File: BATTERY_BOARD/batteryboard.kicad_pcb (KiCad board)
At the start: 2 copper layers, 95.9 x 90.2 mm, 42 parts, among them J1 KEYSTONE-1042, J10 Screw_Terminal_01x02, J11 Screw_Terminal_01x02, J12 Screw_Terminal_01x01, J2 KEYSTONE-1042, J3 KEYSTONE-1042, J4 KEYSTONE-1042, J5 KEYSTONE-1042, J6 KEYSTONE-1042, J7 JST_PH_S2B-PH-SM4, J8 Screw_Terminal_01x02, J9 Screw_Terminal_01x02, Q1 IRF7458, Q2 IRF7458, U1 R5460N233AF

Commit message: Schematic Verified
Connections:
- H1 pad 1: Net-(H1-Pad1) -> unconnected-(H1-Pad1)
- H2 pad 1: Net-(H2-Pad1) -> unconnected-(H2-Pad1)
- H3 pad 1: Net-(H3-Pad1) -> unconnected-(H3-Pad1)
- H4 pad 1: Net-(H4-Pad1) -> unconnected-(H4-Pad1)
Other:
- net class Default removed

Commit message: Battery Board Final Update
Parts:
- removed J12: Screw_Terminal_01x01, Connector_PinHeader_1.00mm:PinHeader_1x01_P1.00mm_Vertical
- removed J9: Screw_Terminal_01x02, custom-footprints:SCREWTERMINAL-3.5MM-2_LOCK
- removed REF** (x6): Fiducial_0.75mm_Mask1.5mm, Fiducial:Fiducial_0.75mm_Mask1.5mm
- removed REF**: JST_PH_B2B-PH-SM4-TB_1x02-1MP_P2.00mm_Vertical, Connector_JST:JST_PH_B2B-PH-SM4-TB_1x02-1MP_P2.00mm_Vertical
- removed Ref**: Val**, custom-footprints:pycubed_logo
- removed Ref** (x2): Val**, custom-footprints:battery_version
- added D1: DFLS130L, mainboard:PWRDI-123, F.Cu at (69.8, 106.1)
- added J13: SM02B-SFHRS-TF_LF__SN_, SamacSys_Parts:SM02BSFHRSTFLFSN, F.Cu at (90.4, 58.7)
- added J14: SM02B-SFHRS-TF_LF__SN_, SamacSys_Parts:SM02BSFHRSTFLFSN, F.Cu at (81.1, 58.7)
- added J15: SM02B-SFHRS-TF_LF__SN_, SamacSys_Parts:SM02BSFHRSTFLFSN, F.Cu at (99.7, 58.7)
- added J16: SM02B-SFHRS-TF_LF__SN_, SamacSys_Parts:SM02BSFHRSTFLFSN, F.Cu at (109.1, 58.7)
- added K1: 9-1462038-9, SamacSys_Parts:914620389, F.Cu at (81.9, 109.5)
- added Q10: IRLML2803, mainboard:SOT-23, F.Cu at (85.9, 95.6)
- added Q11: IRLML2803, mainboard:SOT-23, F.Cu at (121.4, 106.5)
- added Q3: MMBT2222AT, mainboard:SOT-23, F.Cu at (73.4, 107.0)
- added Q4: IRLML2803, mainboard:SOT-23, F.Cu at (69.7, 95.6)
- added Q5: IRLML2803, mainboard:SOT-23, F.Cu at (78.0, 95.6)
- added Q6: NDS8434, mainboard:NDS8434, F.Cu at (66.6, 88.1)
- added Q7: NDS8434, mainboard:NDS8434, F.Cu at (72.9, 88.1)
- added Q8: NDS8434, mainboard:NDS8434, F.Cu at (79.1, 88.1)
- added Q9: NDS8434, mainboard:NDS8434, F.Cu at (85.4, 88.1)
- added R10: 100k, Resistor_SMD:R_0603_1608Metric, F.Cu at (66.8, 93.9)
- added R11: 100k, Resistor_SMD:R_0603_1608Metric, F.Cu at (75.1, 93.9)
- added R12: 100k, Resistor_SMD:R_0603_1608Metric, F.Cu at (83.0, 93.8)
- added R13: 100k, Resistor_SMD:R_0603_1608Metric, F.Cu at (118.5, 104.8)
- added R14: 4.7k, Resistor_SMD:R_0603_1608Metric, F.Cu at (85.0, 99.1)
- added R15: 4.7k, Resistor_SMD:R_0603_1608Metric, F.Cu at (120.4, 110.0)
- added R16: 10k, Resistor_SMD:R_0603_1608Metric, F.Cu at (86.9, 99.1)
- added R17: 10k, Resistor_SMD:R_0603_1608Metric, F.Cu at (122.3, 110.0)
- added R5: 10k, Resistor_SMD:R_0603_1608Metric, F.Cu at (73.4, 109.7)
- added R6: 10k, Resistor_SMD:R_0603_1608Metric, F.Cu at (70.6, 99.1)
- added R7: 10k, Resistor_SMD:R_0603_1608Metric, F.Cu at (79.0, 99.1)
- added R8: 4.7k, Resistor_SMD:R_0603_1608Metric, F.Cu at (68.7, 99.1)
- added R9: 4.7k, Resistor_SMD:R_0603_1608Metric, F.Cu at (77.0, 99.1)
- J10, J8: value Screw_Terminal_01x02 -> SM02B-SFHRS-TF_LF__SN_; footprint custom-footprints:SCREWTERMINAL-3.5MM-2_LOCK -> SamacSys_Parts:SM02BSFHRSTFLFSN
- J11: value Screw_Terminal_01x02 -> F3311A7H121014E200; footprint custom-footprints:SCREWTERMINAL-3.5MM-2_LOCK -> SamacSys_Parts:F3311A7H121014E200
- J7: value JST_PH_S2B-PH-SM4 -> SM02B-SFHRS-TF_LF__SN_; footprint Connector_JST:JST_PH_S2B-PH-SM4-TB_1x02-1MP_P2.00mm_Horizontal -> SamacSys_Parts:SM02BSFHRSTFLFSN
- moved J8 62.5 mm to (66.8, 111.2), turned to 0 degrees
- moved J11 57.2 mm to (65.2, 101.0), turned to -90 degrees
- moved J6 36.2 mm to (101.1, 72.9)
- moved J7 34.6 mm to (129.2, 58.9), turned to -90 degrees
- moved TP3 27.5 mm to (116.2, 66.2)
- moved TH1 19.6 mm to (103.5, 113.2)
- moved TP4 14.5 mm to (134.7, 66.7)
- moved Q2 8.14 mm to (119.6, 87.9)
- moved R1 7.48 mm to (126.3, 100.0)
- moved J10 6.98 mm to (121.9, 58.9), turned to -90 degrees
- moved Q1 6.75 mm to (127.3, 88.0)
- moved R3 6.75 mm to (134.8, 90.6)
- moved C3 6.75 mm to (134.0, 85.4)
- moved C4 5.43 mm to (120.2, 97.8)
- moved C1 5.43 mm to (125.2, 94.5)
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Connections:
- C3 pad 2: PACK- -> GND
- J10 pad 1: PACK+ -> GND
- J10 pad 2: PACK- -> PACK+
- J11 pad 1: PACK+ -> unconnected-(J11-Pad1)
- J11 pad 2: PACK- -> unconnected-(J11-Pad2)
- J7 pad 1: PACK+ -> GND
- J7 pad 2: PACK- -> PACK+
- J8 pad 1: PACK+ -> VBATT
- J8 pad 2: PACK- -> VBATT
- Q2 pad 1: PACK- -> GND
- Q2 pad 2: PACK- -> GND
- Q2 pad 3: PACK- -> GND
- R4 pad 2: PACK- -> GND
- TH1 pad 2: PACK- -> GND
- TP3 pad 1: PACK- -> GND
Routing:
- net ENAB_BURN4: track 0.00 -> 60.3 mm, vias 0 -> 2
- net /VBURN_A_IN: track 0.00 -> 41.7 mm
- net Net-(Q11-D): track 0.00 -> 40.3 mm
- net ENAB_BURN3: track 0.00 -> 24.9 mm, vias 0 -> 2
- net BAT_THERM: track 18.0 -> 41.0 mm, vias 0 -> 1
- net BURN_RELAY_A: track 0.00 -> 16.3 mm, vias 0 -> 2
- net ENAB_BURN2: track 0.00 -> 15.4 mm
- net PACK+: track 24.2 -> 37.6 mm, vias 14 -> 18
- net Net-(Q5-D): track 0.00 -> 8.28 mm
- net Net-(K1-COIL-): track 0.00 -> 8.14 mm
- net GND: track 0.00 -> 7.73 mm
- net Net-(Q10-D): track 0.00 -> 7.73 mm
- net Net-(Q4-D): track 0.00 -> 7.41 mm
- net ENAB_BURN1: track 0.00 -> 5.01 mm
- net BM: track 60.5 -> 64.6 mm
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- added copper zone on F.Cu, net /VBURN1
- added copper zone on F.Cu, net /VBURN2
- added copper zone on F.Cu, net /VBURN3
- added copper zone on F.Cu, net /VBURN4
- added copper zone on F.Cu, net /VBURN_A_IN
- added copper zone on F.Cu, net GND
- added copper zone on F.Cu, net VBATT
- removed copper zone on F.Cu, net PACK-
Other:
- outline, holes or cut-outs redrawn
- board text added: "+ -"
- board text removed: "+"
- board text removed: "-"
- board text removed: "1. CHECK CELL POLARITY BEFORE INSTALLING IN TO PACK 2. INSTALL CELLS IN NUMERICAL ORDER AS INDICATED (J1,2,3,etc...) 3. IF 0V OUTPUT, CHECK CELL BALANCE"
- board text removed: "P-"
- board text removed: "RBF PORT SIDE"

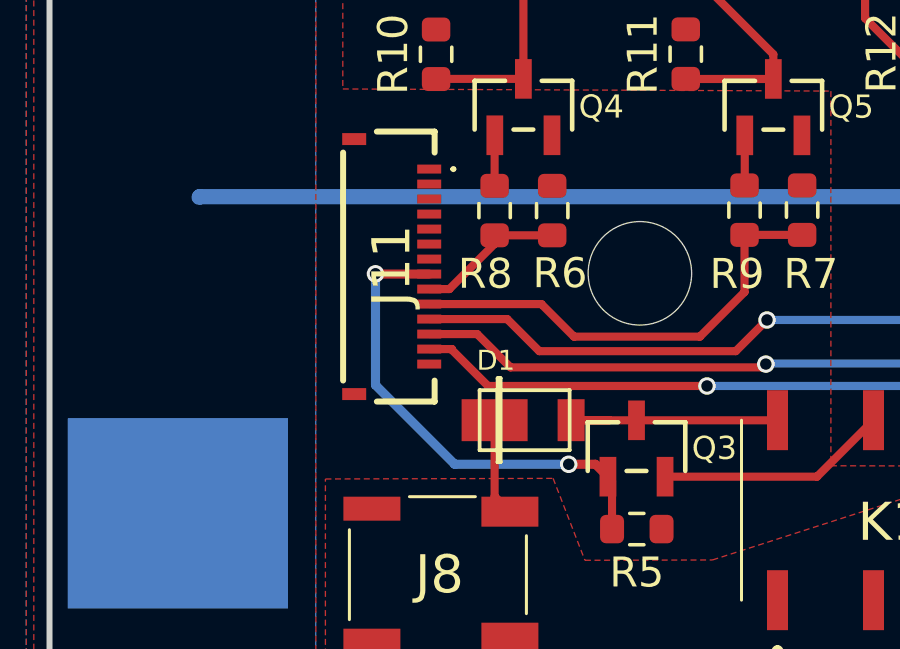
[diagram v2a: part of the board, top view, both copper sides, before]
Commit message: Updated the FPC Connections
FPC connector is reversable now
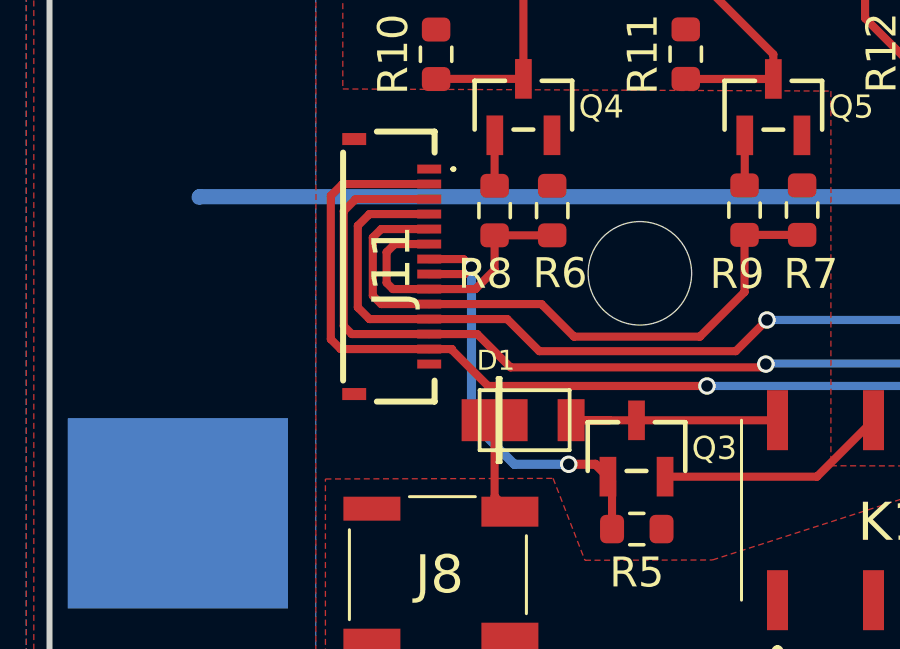
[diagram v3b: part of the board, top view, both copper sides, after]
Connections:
- J11 pad 1: unconnected-(J11-Pad1) -> GND
- J11 pad 2: unconnected-(J11-Pad2) -> BAT_THERM
- J11 pad 3: unconnected-(J11-Pad3) -> ENAB_BURN4
- J11 pad 4: unconnected-(J11-Pad4) -> ENAB_BURN3
- J11 pad 5: unconnected-(J11-Pad5) -> ENAB_BURN2
- J11 pad 6: unconnected-(J11-Pad6) -> ENAB_BURN1
- J11 pad 7: GND -> BURN_RELAY_A
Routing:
- net BAT_THERM: track 41.0 -> 52.7 mm
- net ENAB_BURN4: track 60.3 -> 70.1 mm
- net ENAB_BURN3: track 24.9 -> 32.7 mm
- net ENAB_BURN2: track 15.4 -> 21.3 mm
- net ENAB_BURN1: track 5.01 -> 9.58 mm
- net BURN_RELAY_A: track 16.3 -> 15.3 mm

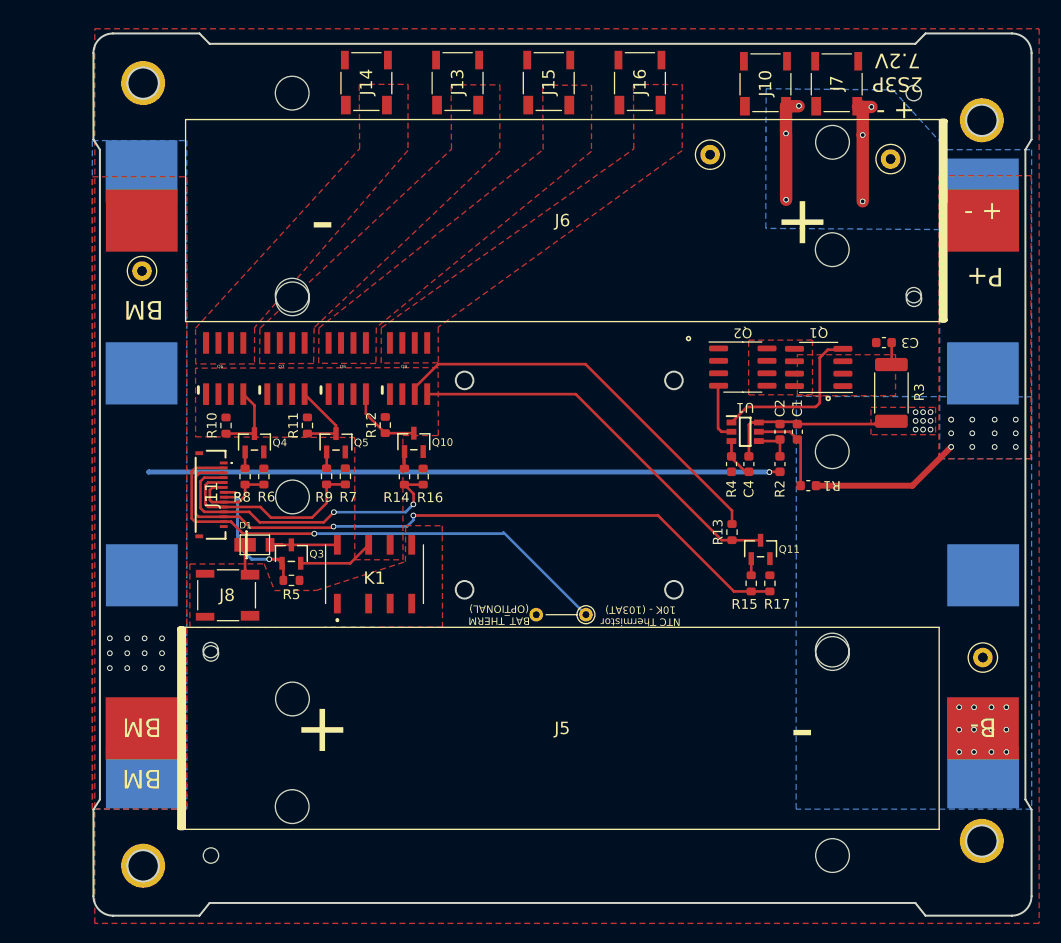
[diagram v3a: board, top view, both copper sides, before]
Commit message: Battery Board Updated based on Feedback
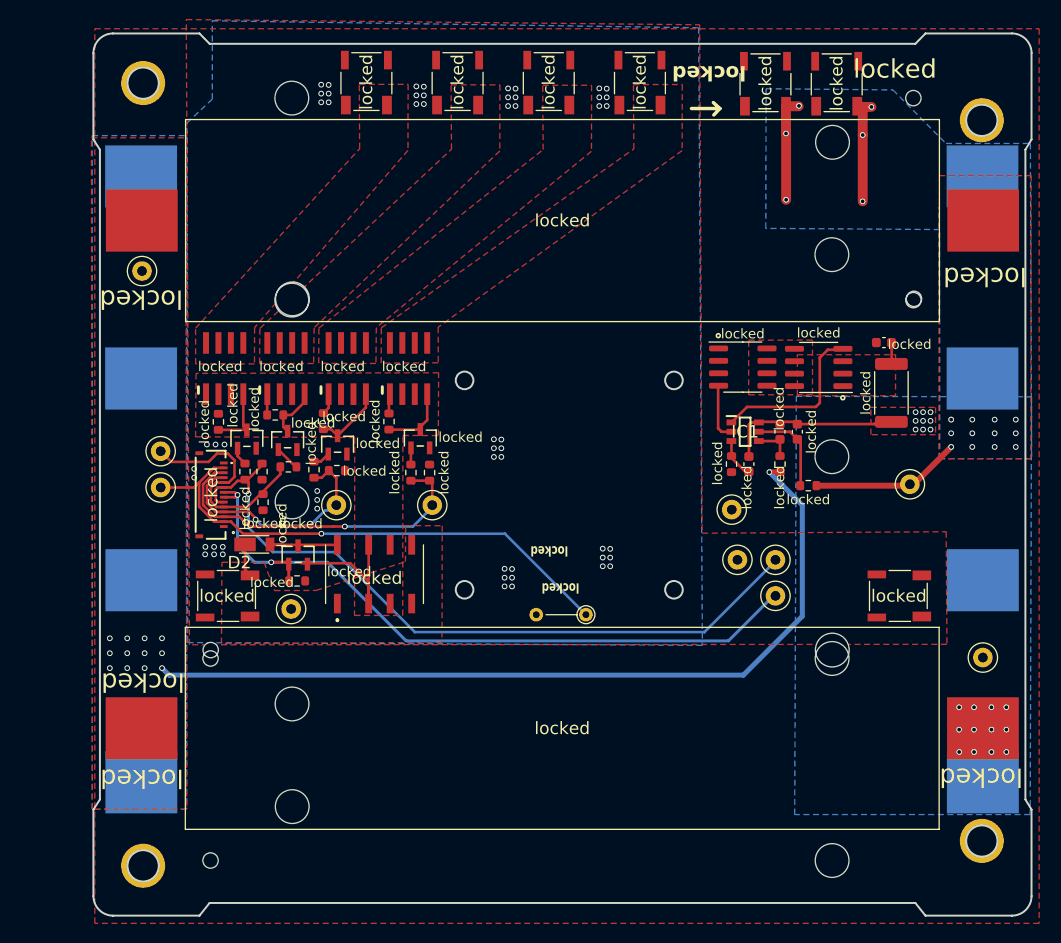
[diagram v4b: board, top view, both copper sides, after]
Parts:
- removed D1: DFLS130L, mainboard:PWRDI-123
- removed U1: R5460N233AF, custom-footprints:SOT95P280X130-6N
- added D2: DFLS130L-7, SamacSys_Parts:POWERDI_123, F.Cu at (70.3, 106.0)
- added IC1: R5460N233AF-TR-FE, SamacSys_Parts:SOT95P280X140-6N, F.Cu at (119.8, 94.5)
- added TP10: TestPoint, TestPoint:TestPoint_Loop_D1.80mm_Drill1.0mm_Beaded, F.Cu at (78.0, 102.0)
- added TP11: TestPoint, TestPoint:TestPoint_Loop_D1.80mm_Drill1.0mm_Beaded, F.Cu at (87.8, 102.0)
- added TP12: TestPoint, TestPoint:TestPoint_Loop_D1.80mm_Drill1.0mm_Beaded, F.Cu at (60.1, 100.2)
- added TP5: TestPoint, TestPoint:TestPoint_Loop_D1.80mm_Drill1.0mm_Beaded, F.Cu at (119.0, 107.6)
- added TP6: TestPoint, TestPoint:TestPoint_Loop_D1.80mm_Drill1.0mm_Beaded, F.Cu at (73.4, 112.6)
- added TP7: TestPoint, TestPoint:TestPoint_Loop_D1.80mm_Drill1.0mm_Beaded, F.Cu at (122.9, 111.3)
- added TP8: TestPoint, TestPoint:TestPoint_Loop_D1.80mm_Drill1.0mm_Beaded, F.Cu at (122.9, 107.6)
- added TP9: TestPoint, TestPoint:TestPoint_Loop_D1.80mm_Drill1.0mm_Beaded, F.Cu at (60.1, 96.5)
- added locked: SM02B-SFHRS-TF_LF__SN_, SamacSys_Parts:SM02BSFHRSTFLFSN, F.Cu at (135.5, 111.3)
- locked: renamed from J5; value KEYSTONE-1042 -> 1042; footprint custom-footprints:KEYSTONE-1042 -> SamacSys_Parts:KEYSTONE-1042
- locked: renamed from J6; value KEYSTONE-1042 -> 1042; footprint custom-footprints:KEYSTONE-1042 -> SamacSys_Parts:KEYSTONE-1042
- locked: renamed from J2; value KEYSTONE-1042 -> 1042; footprint custom-footprints:KEYSTONE-1042 -> SamacSys_Parts:KEYSTONE-1042
- locked: renamed from J1; value KEYSTONE-1042 -> 1042; footprint custom-footprints:KEYSTONE-1042 -> SamacSys_Parts:KEYSTONE-1042
- locked: renamed from J3; value KEYSTONE-1042 -> 1042; footprint custom-footprints:KEYSTONE-1042 -> SamacSys_Parts:KEYSTONE-1042
- locked: renamed from J4; value KEYSTONE-1042 -> 1042; footprint custom-footprints:KEYSTONE-1042 -> SamacSys_Parts:KEYSTONE-1042
- moved locked 36.8 mm to (83.4, 93.5)
- moved locked 36.6 mm to (85.6, 98.7)
- moved locked 36.6 mm to (87.6, 98.7)
- moved locked 36.6 mm to (86.6, 95.2)
- moved TP3 36.3 mm to (118.4, 102.5)
- moved TP4 33.3 mm to (136.7, 99.9)
- moved locked 9.27 mm to (75.7, 98.4)
- moved locked 8.84 mm to (78.1, 98.5), turned to 0 degrees
- moved locked 8.82 mm to (70.5, 101.7), turned to -90 degrees
- moved locked 7.80 mm to (78.2, 95.8)
- moved locked 6.33 mm to (76.7, 93.4)
- moved locked 4.95 mm to (73.1, 95.4)
- moved locked 4.02 mm to (73.1, 98.1), turned to 180 degrees
- moved locked 3.46 mm to (71.8, 92.8), turned to 180 degrees
- moved locked 0.86 mm to (66.0, 93.5)
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- renumbered Q1 to locked, R4 to locked, R3 to locked, J7 to locked, K1 to locked, Q6 to locked, R6 to locked, J13 to locked, R7 to locked, R16 to locked, R12 to locked, Q7 to locked, R11 to locked, J16 to locked, R13 to locked, R14 to locked, J8 to locked, Q3 to locked, R17 to locked, R15 to locked, C1 to locked, Q10 to locked, J14 to locked, J11 to locked, Q5 to locked, Q9 to locked, R10 to locked, J15 to locked, R9 to locked, Q8 to locked, C2 to locked, R5 to locked, R8 to locked, Q4 to locked, Q11 to locked, J10 to locked, C4 to locked, C3 to locked, R1 to locked, R2 to locked, Q2 to locked
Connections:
- TP3 pad 1: GND -> PACK-
- locked pad 2: GND -> PACK- (x3)
- locked pad 1: GND -> PACK- (x3)
- locked pad 3: unconnected-(J7-Pad3) -> PACK-
- locked pad 4: unconnected-(J7-Pad4) -> PACK-
- locked pad 2: unconnected-(K1-NC_1-Pad2) -> GND
- locked pad 3: unconnected-(K1-COM_1-Pad3) -> /VBURN_A_IN
- locked pad 4: unconnected-(K1-NO_1-Pad4) -> VBATT
- locked pad 3: unconnected-(J8-Pad3) -> GND
- locked pad 4: unconnected-(J8-Pad4) -> GND
- locked pad MP1: unconnected-(J11-PadMP1) -> GND
- locked pad MP2: unconnected-(J11-PadMP2) -> GND
- locked pad 3: unconnected-(J10-Pad3) -> PACK-
- locked pad 4: unconnected-(J10-Pad4) -> PACK-
- locked pad 3: GND -> PACK-
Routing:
- net ENAB_BURN1: track 9.58 -> 74.7 mm, vias 0 -> 1
- net BURN_RELAY_A: track 15.3 -> 72.8 mm
- net /VBURN_A_IN: track 41.7 -> 6.30 mm
- net ENAB_BURN4: track 70.1 -> 35.0 mm, vias 2 -> 1
- net Net-(Q11-D): track 40.3 -> 6.96 mm
- net BM: track 64.6 -> 85.5 mm
- net GND: track 7.73 -> 16.0 mm, vias 0 -> 56
- net ENAB_BURN3: track 32.7 -> 24.7 mm, vias 2 -> 1
- net ENAB_BURN2: track 21.3 -> 24.2 mm
- net Net-(Q5-D): track 8.28 -> 5.45 mm
- net BAT_THERM: track 52.7 -> 53.9 mm
- net Net-(Q5-G): track 1.67 -> 2.58 mm
- net Net-(Q4-D): track 7.41 -> 6.71 mm
- net Net-(Q10-D): track 7.73 -> 7.17 mm
- added copper zone on B.Cu, net GND
- added copper zone on F.Cu, net PACK-
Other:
- board text added: "locked"
- board text removed: "+ -"
- board text removed: "- +"
- board text removed: "2S3P 7.2V"
- board text removed: "B-"
- board text removed: "BAT_THERM (OPTIONAL)"
- board text removed: "BM"
- board text removed: "HOLLIDAY"
- board text removed: "NTC Thermistor 10K - (103AT)"
- board text removed: "P+"

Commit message: Battery Board all changes done
Based on feedback by Neil
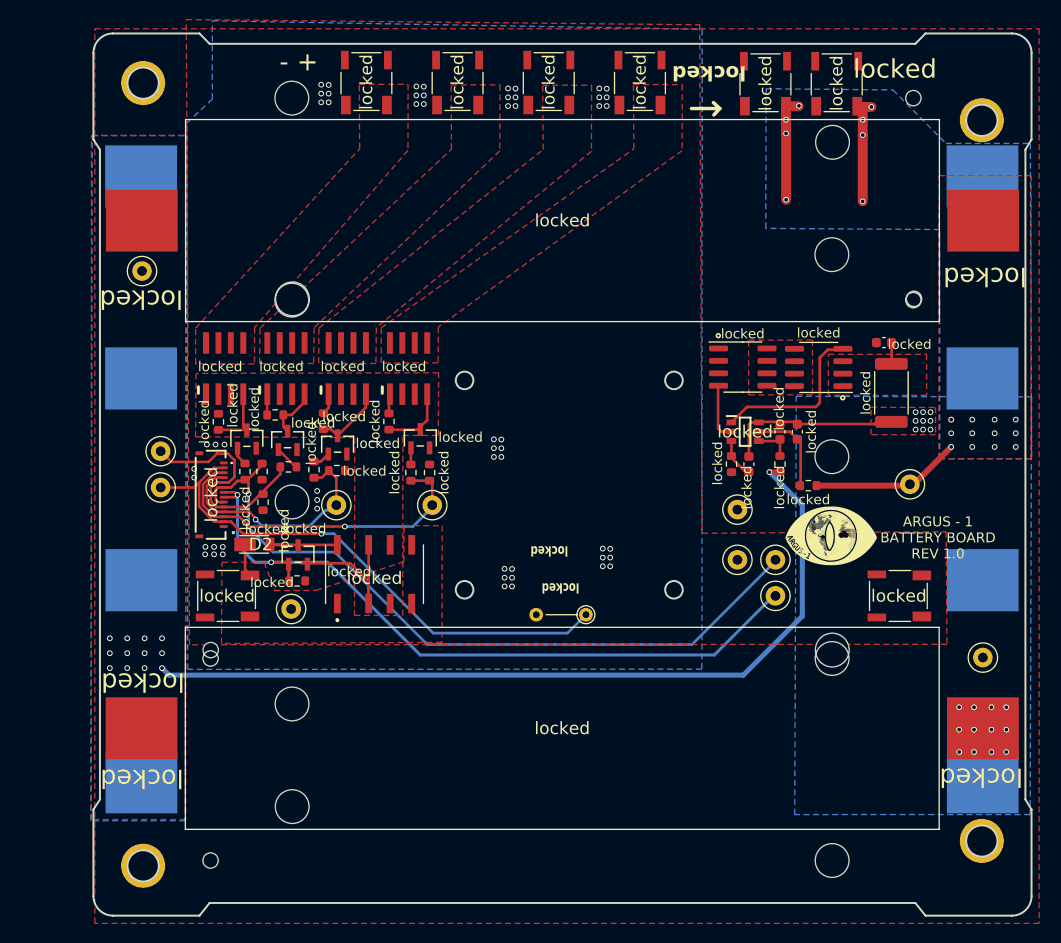
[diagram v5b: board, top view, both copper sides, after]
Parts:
- added G***: LOGO, Symbol:Argus LOGO 10x6.4, F.Cu at (128.5, 105.1)
- added G***: LOGO, Symbol:Argus LOGO 10x6.4, B.Cu at (76.4, 68.1)
- H3: moved to B.Cu
- moved TP3 0.58 mm to (119.0, 102.5)
- turned H3 to 180 degrees
- renumbered IC1 to locked
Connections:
- locked pad 3: unconnected-(J13-Pad3) -> GND
- locked pad 4: unconnected-(J13-Pad4) -> GND
- locked pad 3: unconnected-(J16-Pad3) -> GND
- locked pad 4: unconnected-(J16-Pad4) -> GND
- locked pad 3: unconnected-(J14-Pad3) -> GND
- locked pad 4: unconnected-(J14-Pad4) -> GND
- locked pad 3: unconnected-(J15-Pad3) -> GND
- locked pad 4: unconnected-(J15-Pad4) -> GND
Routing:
- net BAT_THERM: track 53.9 -> 55.4 mm
- net BURN_RELAY_A: track 72.8 -> 74.0 mm
- net ENAB_BURN1: track 74.7 -> 75.8 mm
- net PACK+: vias 18 -> 20
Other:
- board text added: "- +"
- board text added: "ARGUS - 1 BATTERY BOARD REV 1.0"
